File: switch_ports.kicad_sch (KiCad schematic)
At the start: 76 parts, among them J2 Conn_01x04, J3 Conn_01x04, J5 Conn_01x04, J7 Conn_01x04, U1 RTL8367RB

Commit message: Finish routing for the most part
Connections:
- net P1GRN: now also R21.1; no longer R21.1
- net P1YLW: now also R21.1; no longer R21.1
- net P2GRN: now also R21.1; no longer R21.1
- net P2YLW: now also R21.1; no longer R21.1
- net P3GRN: now also R21.1; no longer R21.1
- net P3YLW: now also R21.1; no longer R21.1
- net P4YLW: now also R21.1; no longer R21.1
- net at R21.2: now also J1.10; no longer J1.12 (x2)
- net at R21.2: now also J1.12; no longer J1.10 (x2)
- net at R21.2: now also J1.10; no longer J1.10 (x2)
- net at R21.2: now also J1.12; no longer J1.12
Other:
- moved on the sheet: R21
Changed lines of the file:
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@@
     )
   )
-  (symbol (lib_id "Device:R_Small") (at 139.7 120.65 0) (unit 1)
-    (in_bom yes) (on_board yes) (dnp no)
-    (property "Reference" "R21" (at 141.1986 119.626 0)
-      (effects (font (size 1.27 1.27)) (justify left))
-    )
-    (property "Value" "2.2k" (at 141.1986 121.674 0)
-      (effects (font (size 1.27 1.27)) (justify left))
-    )
-    (property "Footprint" "Resistor_SMD:R_0402_1005Metric" (at 139.7 120.65 0)
-      (effects (font (size 1.27 1.27)) hide)
-    )
-    (property "Datasheet" "~" (at 139.7 120.65 0)
-      (effects (font (size 1.27 1.27)) hide)
-    )
-    (property "LCSC" "C25879" (at 139.7 120.65 0)
+  (symbol (lib_id "Device:R_Small") (at 137.16 105.41 0) (unit 1)
+    (in_bom yes) (on_board yes) (dnp no)
+    (property "Reference" "R21" (at 138.6586 104.386 0)
+      (effects (font (size 1.27 1.27)) (justify left))
+    )
+    (property "Value" "2.2k" (at 138.6586 106.434 0)
+      (effects (font (size 1.27 1.27)) (justify left))
+    )
+    (property "Footprint" "Resistor_SMD:R_0402_1005Metric" (at 137.16 105.41 0)
+      (effects (font (size 1.27 1.27)) hide)
+    )
+    (property "Datasheet" "~" (at 137.16 105.41 0)
+      (effects (font (size 1.27 1.27)) hide)
+    )
+    (property "LCSC" "C25879" (at 137.16 105.41 0)
       (effects (font (size 1.27 1.27)) hide)
     )
@@
     )
   )
-  (symbol (lib_id "Device:R_Small") (at 273.05 105.41 0) (unit 1)
-    (in_bom yes) (on_board yes) (dnp no)
-    (property "Reference" "R21" (at 274.5486 104.386 0)
-      (effects (font (size 1.27 1.27)) (justify left))
-    )
-    (property "Value" "2.2k" (at 274.5486 106.434 0)
-      (effects (font (size 1.27 1.27)) (justify left))
-    )
-    (property "Footprint" "Resistor_SMD:R_0402_1005Metric" (at 273.05 105.41 0)
-      (effects (font (size 1.27 1.27)) hide)
-    )
-    (property "Datasheet" "~" (at 273.05 105.41 0)
-      (effects (font (size 1.27 1.27)) hide)
-    )
-    (property "LCSC" "C25879" (at 273.05 105.41 0)
+  (symbol (lib_id "Device:R_Small") (at 275.59 120.65 0) (unit 1)
+    (in_bom yes) (on_board yes) (dnp no)
+    (property "Reference" "R21" (at 277.0886 119.626 0)
+      (effects (font (size 1.27 1.27)) (justify left))
+    )
+    (property "Value" "2.2k" (at 277.0886 121.674 0)
+      (effects (font (size 1.27 1.27)) (justify left))
+    )
+    (property "Footprint" "Resistor_SMD:R_0402_1005Metric" (at 275.59 120.65 0)
+      (effects (font (size 1.27 1.27)) hide)
+    )
+    (property "Datasheet" "~" (at 275.59 120.65 0)
+      (effects (font (size 1.27 1.27)) hide)
+    )
+    (property "LCSC" "C25879" (at 275.59 120.65 0)
       (effects (font (size 1.27 1.27)) hide)
     )
@@
     )
   )
-  (symbol (lib_id "Device:R_Small") (at 275.59 120.65 0) (unit 1)
-    (in_bom yes) (on_board yes) (dnp no)
-    (property "Reference" "R21" (at 277.0886 119.626 0)
-      (effects (font (size 1.27 1.27)) (justify left))
-    )
-    (property "Value" "2.2k" (at 277.0886 121.674 0)
-      (effects (font (size 1.27 1.27)) (justify left))
-    )
-    (property "Footprint" "Resistor_SMD:R_0402_1005Metric" (at 275.59 120.65 0)
-      (effects (font (size 1.27 1.27)) hide)
-    )
-    (property "Datasheet" "~" (at 275.59 120.65 0)
-      (effects (font (size 1.27 1.27)) hide)
-    )
-    (property "LCSC" "C25879" (at 275.59 120.65 0)
+  (symbol (lib_id "Device:R_Small") (at 273.05 105.41 0) (unit 1)
+    (in_bom yes) (on_board yes) (dnp no)
+    (property "Reference" "R21" (at 274.5486 104.386 0)
+      (effects (font (size 1.27 1.27)) (justify left))
+    )
+    (property "Value" "2.2k" (at 274.5486 106.434 0)
+      (effects (font (size 1.27 1.27)) (justify left))
+    )
+    (property "Footprint" "Resistor_SMD:R_0402_1005Metric" (at 273.05 105.41 0)
+      (effects (font (size 1.27 1.27)) hide)
+    )
+    (property "Datasheet" "~" (at 273.05 105.41 0)
+      (effects (font (size 1.27 1.27)) hide)
+    )
+    (property "LCSC" "C25879" (at 273.05 105.41 0)
       (effects (font (size 1.27 1.27)) hide)
     )
@@
     )
   )
-  (symbol (lib_id "Device:R_Small") (at 273.05 27.94 0) (unit 1)
-    (in_bom yes) (on_board yes) (dnp no)
-    (property "Reference" "R21" (at 274.5486 26.916 0)
-      (effects (font (size 1.27 1.27)) (justify left))
-    )
-    (property "Value" "2.2k" (at 274.5486 28.964 0)
-      (effects (font (size 1.27 1.27)) (justify left))
-    )
-    (property "Footprint" "Resistor_SMD:R_0402_1005Metric" (at 273.05 27.94 0)
-      (effects (font (size 1.27 1.27)) hide)
-    )
-    (property "Datasheet" "~" (at 273.05 27.94 0)
-      (effects (font (size 1.27 1.27)) hide)
-    )
-    (property "LCSC" "C25879" (at 273.05 27.94 0)
+  (symbol (lib_id "Device:R_Small") (at 137.16 27.94 0) (unit 1)
+    (in_bom yes) (on_board yes) (dnp no)
+    (property "Reference" "R21" (at 138.6586 26.916 0)
+      (effects (font (size 1.27 1.27)) (justify left))
+    )
+    (property "Value" "2.2k" (at 138.6586 28.964 0)
+      (effects (font (size 1.27 1.27)) (justify left))
+    )
+    (property "Footprint" "Resistor_SMD:R_0402_1005Metric" (at 137.16 27.94 0)
+      (effects (font (size 1.27 1.27)) hide)
+    )
+    (property "Datasheet" "~" (at 137.16 27.94 0)
+      (effects (font (size 1.27 1.27)) hide)
+    )
+    (property "LCSC" "C25879" (at 137.16 27.94 0)
       (effects (font (size 1.27 1.27)) hide)
     )
@@
     )
   )
-  (symbol (lib_id "Device:R_Small") (at 275.59 43.18 0) (unit 1)
-    (in_bom yes) (on_board yes) (dnp no)
-    (property "Reference" "R21" (at 277.0886 42.156 0)
-      (effects (font (size 1.27 1.27)) (justify left))
-    )
-    (property "Value" "2.2k" (at 277.0886 44.204 0)
-      (effects (font (size 1.27 1.27)) (justify left))
-    )
-    (property "Footprint" "Resistor_SMD:R_0402_1005Metric" (at 275.59 43.18 0)
-      (effects (font (size 1.27 1.27)) hide)
-    )
-    (property "Datasheet" "~" (at 275.59 43.18 0)
-      (effects (font (size 1.27 1.27)) hide)
-    )
-    (property "LCSC" "C25879" (at 275.59 43.18 0)
+  (symbol (lib_id "Device:R_Small") (at 139.7 120.65 0) (unit 1)
+    (in_bom yes) (on_board yes) (dnp no)
+    (property "Reference" "R21" (at 141.1986 119.626 0)
+      (effects (font (size 1.27 1.27)) (justify left))
+    )
+    (property "Value" "2.2k" (at 141.1986 121.674 0)
+      (effects (font (size 1.27 1.27)) (justify left))
+    )
+    (property "Footprint" "Resistor_SMD:R_0402_1005Metric" (at 139.7 120.65 0)
+      (effects (font (size 1.27 1.27)) hide)
+    )
+    (property "Datasheet" "~" (at 139.7 120.65 0)
+      (effects (font (size 1.27 1.27)) hide)
+    )
+    (property "LCSC" "C25879" (at 139.7 120.65 0)
       (effects (font (size 1.27 1.27)) hide)
     )
@@
     )
   )
-  (symbol (lib_id "Device:R_Small") (at 137.16 27.94 0) (unit 1)
-    (in_bom yes) (on_board yes) (dnp no)
-    (property "Reference" "R21" (at 138.6586 26.916 0)
-      (effects (font (size 1.27 1.27)) (justify left))
-    )
-    (property "Value" "2.2k" (at 138.6586 28.964 0)
-      (effects (font (size 1.27 1.27)) (justify left))
-    )
-    (property "Footprint" "Resistor_SMD:R_0402_1005Metric" (at 137.16 27.94 0)
-      (effects (font (size 1.27 1.27)) hide)
-    )
-    (property "Datasheet" "~" (at 137.16 27.94 0)
-      (effects (font (size 1.27 1.27)) hide)
-    )
-    (property "LCSC" "C25879" (at 137.16 27.94 0)
+  (symbol (lib_id "Device:R_Small") (at 275.59 43.18 0) (unit 1)
+    (in_bom yes) (on_board yes) (dnp no)
+    (property "Reference" "R21" (at 277.0886 42.156 0)
+      (effects (font (size 1.27 1.27)) (justify left))
+    )
+    (property "Value" "2.2k" (at 277.0886 44.204 0)
+      (effects (font (size 1.27 1.27)) (justify left))
+    )
+    (property "Footprint" "Resistor_SMD:R_0402_1005Metric" (at 275.59 43.18 0)
+      (effects (font (size 1.27 1.27)) hide)
+    )
+    (property "Datasheet" "~" (at 275.59 43.18 0)
+      (effects (font (size 1.27 1.27)) hide)
+    )
+    (property "LCSC" "C25879" (at 275.59 43.18 0)
       (effects (font (size 1.27 1.27)) hide)
     )
@@
     )
   )
-  (symbol (lib_id "Device:R_Small") (at 137.16 105.41 0) (unit 1)
-    (in_bom yes) (on_board yes) (dnp no)
-    (property "Reference" "R21" (at 138.6586 104.386 0)
-      (effects (font (size 1.27 1.27)) (justify left))
-    )
-    (property "Value" "2.2k" (at 138.6586 106.434 0)
-      (effects (font (size 1.27 1.27)) (justify left))
-    )
-    (property "Footprint" "Resistor_SMD:R_0402_1005Metric" (at 137.16 105.41 0)
-      (effects (font (size 1.27 1.27)) hide)
-    )
-    (property "Datasheet" "~" (at 137.16 105.41 0)
-      (effects (font (size 1.27 1.27)) hide)
-    )
-    (property "LCSC" "C25879" (at 137.16 105.41 0)
-      (effects (font (size 1.27 1.27)) hide)
-    )
+  (symbol (lib_id "Device:R_Small") (at 273.05 27.94 0) (unit 1)
+    (in_bom yes) (on_board yes) (dnp no)
+    (property "Reference" "R21" (at 274.5486 26.916 0)
+      (effects (font (size 1.27 1.27)) (justify left))
+    )
+    (property "Value" "2.2k" (at 274.5486 28.964 0)
+      (effects (font (size 1.27 1.27)) (justify left))
+    )
+    (property "Footprint" "Resistor_SMD:R_0402_1005Metric" (at 273.05 27.94 0)
+      (effects (font (size 1.27 1.27)) hide)
+    )
+    (property "Datasheet" "~" (at 273.05 27.94 0)
+      (effects (font (size 1.27 1.27)) hide)
+    )
+    (property "LCSC" "C25879" (at 273.05 27.94 0)
+      (effects (font (size 1.27 1.27)) hide)
+    )

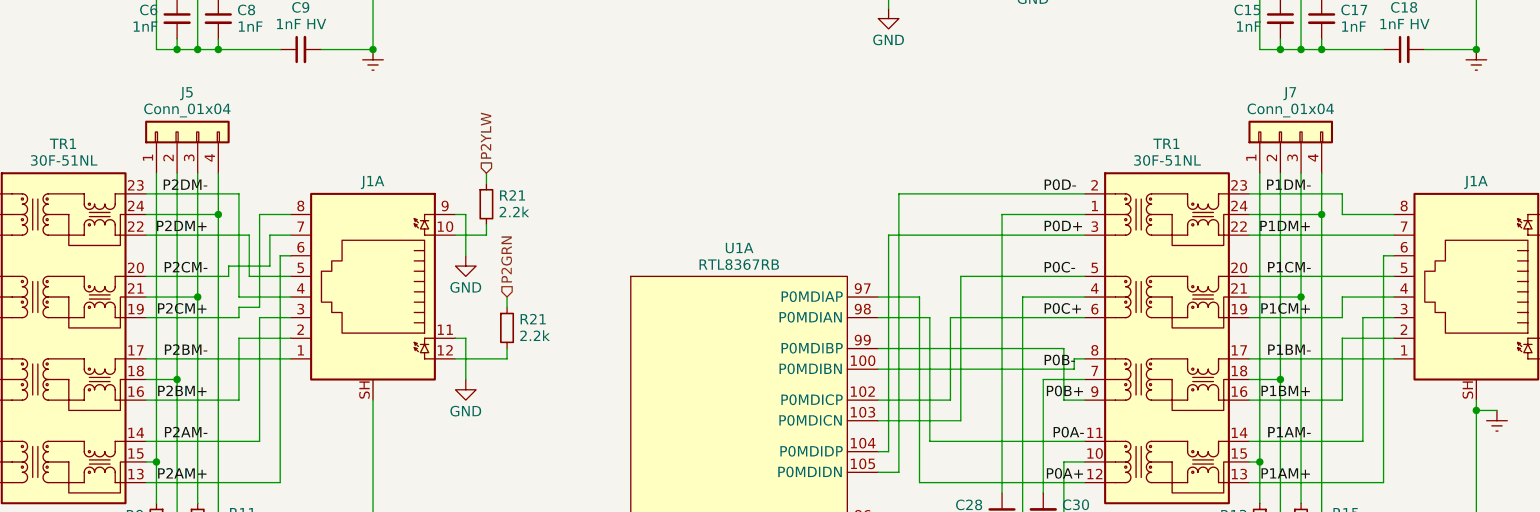
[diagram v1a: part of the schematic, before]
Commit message: Finish signal routing
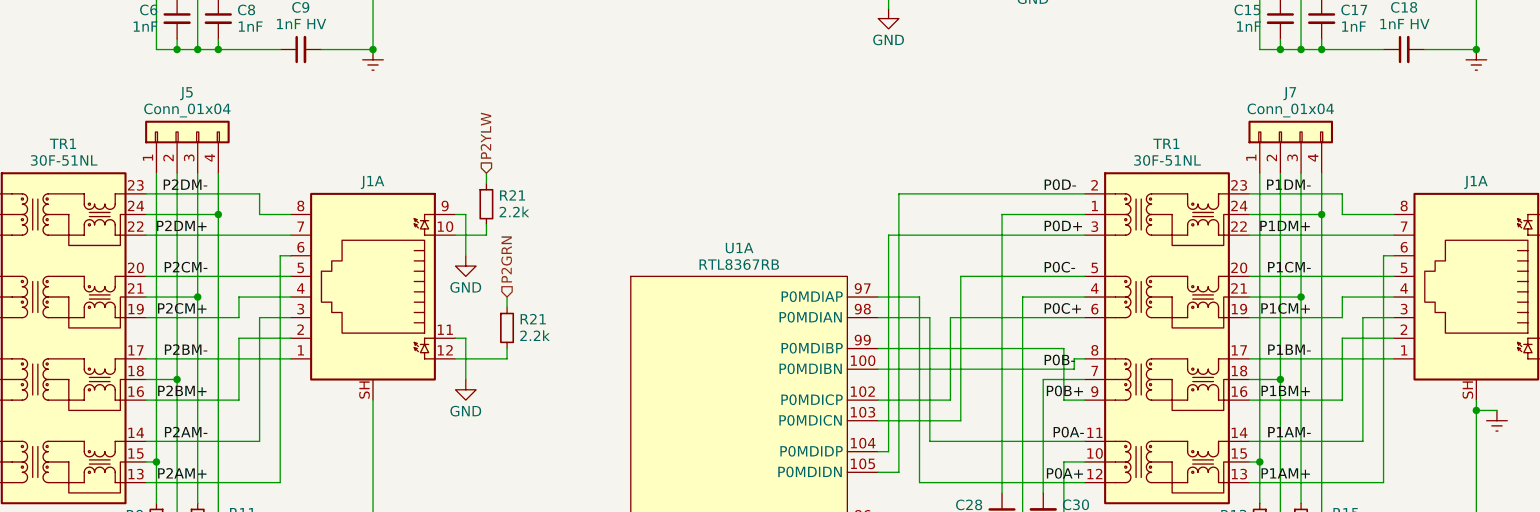
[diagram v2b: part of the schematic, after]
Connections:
- net P2CM+: now also J1.4; no longer J1.8
- net P2CM-: now also J1.5; no longer J1.7
- net P2DM+: now also J1.7; no longer J1.5
- net P2DM-: now also J1.8; no longer J1.4

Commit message: Fix LCSC part numbers
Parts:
- J2, J3, J5, J7: LCSC C780062 -> C5346656
- R2: LCSC (none) -> C25133
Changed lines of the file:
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@@
       (effects (font (size 1.27 1.27)) hide)
     )
-    (property "LCSC" "C780062" (at 234.95 96.52 90)
+    (property "LCSC" "C5346656" (at 234.95 96.52 90)
       (effects (font (size 1.27 1.27)) hide)
     )
@@
       (effects (font (size 1.27 1.27)) hide)
     )
-    (property "LCSC" "C780062" (at 99.06 19.05 90)
+    (property "LCSC" "C5346656" (at 99.06 19.05 90)
       (effects (font (size 1.27 1.27)) hide)
     )
@@
       (effects (font (size 1.27 1.27)) hide)
     )
-    (property "Datasheet" "C25133" (at 96.52 67.31 0)
+    (property "Datasheet" "" (at 96.52 67.31 0)
+      (effects (font (size 1.27 1.27)) hide)
+    )
+    (property "LCSC" "C25133" (at 96.52 67.31 0)
       (effects (font (size 1.27 1.27)) hide)
     )
@@
       (effects (font (size 1.27 1.27)) hide)
     )
-    (property "LCSC" "C780062" (at 234.95 19.05 90)
+    (property "LCSC" "C5346656" (at 234.95 19.05 90)
       (effects (font (size 1.27 1.27)) hide)
     )
@@
       (effects (font (size 1.27 1.27)) hide)
     )
-    (property "LCSC" "C780062" (at 99.06 96.52 90)
-      (effects (font (size 1.27 1.27)) hide)
-    )
+    (property "LCSC" "C5346656" (at 99.06 96.52 90)
+      (effects (font (size 1.27 1.27)) hide)
+    )
